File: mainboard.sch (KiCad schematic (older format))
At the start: 69 parts, among them J1 Conn_01x06, J2 USB_B_Micro, J3 xf2m-2415-1a, J4 XF2M-1015-1A, J5 Conn_01x02, J6 U.FL-R-SMT-1, J7 Conn_02x02_Top_Bottom, J8 Micro_SD_Card, SW1 KMR231NG LFS, U1 BMX160, U11 AP2112K-3.3, U2 MAX708RESA-T, U3 ATSAMD51J20A-M, U4 DRV8830DRC, U5 MR25H40, U6 DRV8830DRC, U8 DRV8830DRC, U9 RFM98PW-symbols, Y1 Crystal

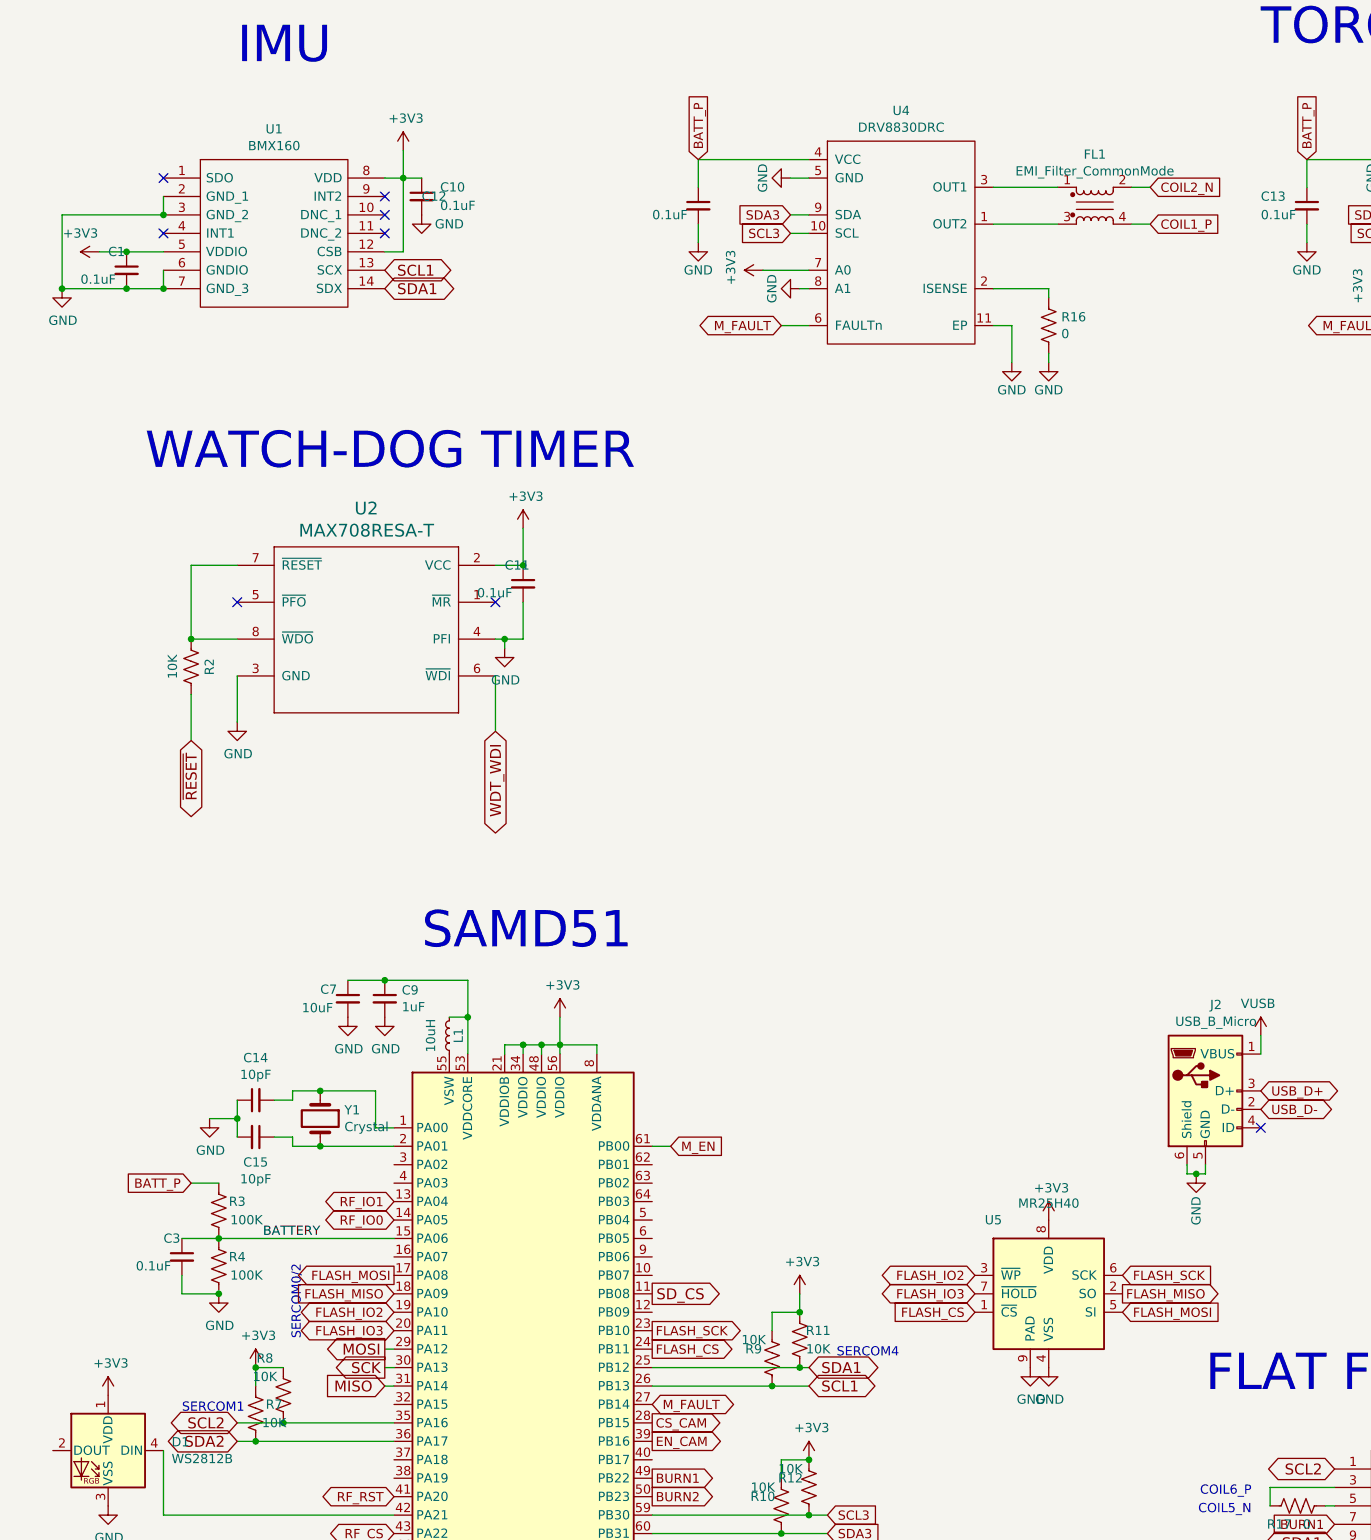
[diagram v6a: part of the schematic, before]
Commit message: ran DRC & added pullups
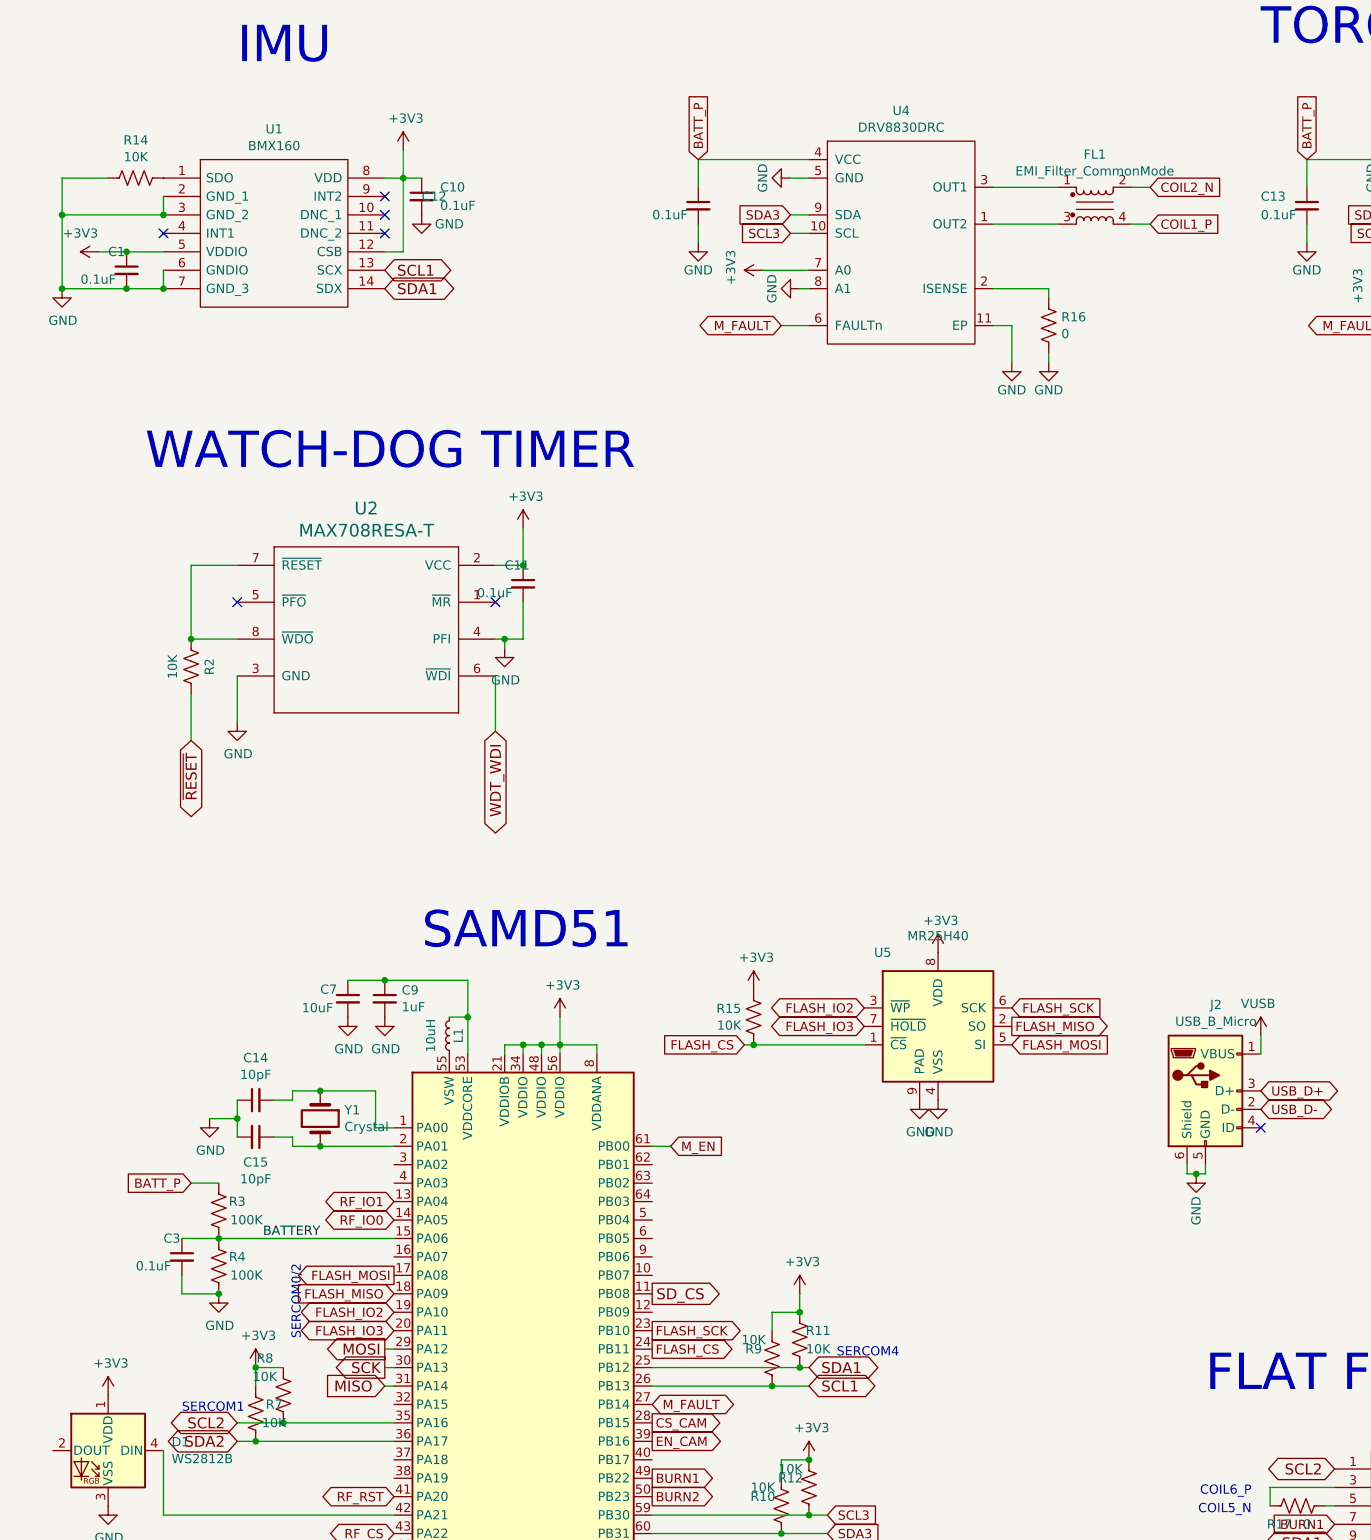
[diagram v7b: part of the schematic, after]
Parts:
- added R14, R15: 10K, Resistor_SMD:R_0402_1005Metric, symbol mainboard-rescue:R_US-Device
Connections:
- net +3V3: now also R15.1
- net FLASH_CS: now also R15.2
- net GND: now also R14.1
- net at U1.1 (SDO): now also R14.2
- no-connect marks 10 -> 9
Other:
- moved on the sheet: U5
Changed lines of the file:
@@
 Wire Wire Line
 	2500 1750 2400 1750
-NoConn ~ 1200 1750
 $Comp
 L mainboard-rescue:R_US-Device R19
@@
 L Memory_NVRAM:MR25H40 U5
 U 1 1 5F5B5E9E
-P 6000 7800
-F 0 "U5" H 5700 8200 50  0000 C CNN
-F 1 "MR25H40" H 6000 8290 50  0000 C CNN
-F 2 "MR25H40:SON127P600X500X90-9N" H 6000 7800 50  0001 C CNN
-F 3 "https://www.everspin.com/file/217/download" H 5700 8100 50  0001 C CNN
-	1    6000 7800
-	1    0    0    -1
-$EndComp
-Text GLabel 5600 7900 0    50   Input ~ 0
+P 5400 6350
+F 0 "U5" H 5100 6750 50  0000 C CNN
+F 1 "MR25H40" H 5400 6840 50  0000 C CNN
+F 2 "MR25H40:SON127P600X500X90-9N" H 5400 6350 50  0001 C CNN
+F 3 "https://www.everspin.com/file/217/download" H 5100 6650 50  0001 C CNN
+	1    5400 6350
+	1    0    0    -1
+$EndComp
+Text GLabel 4350 6450 0    50   Input ~ 0
 FLASH_CS
-Text GLabel 6400 7700 2    50   Input ~ 0
+Text GLabel 5800 6250 2    50   Input ~ 0
 FLASH_SCK
 $Comp
 L power:+3V3 #PWR036
 U 1 1 5F5BBCEF
-P 6000 7400
-F 0 "#PWR036" H 6000 7250 50  0001 C CNN
-F 1 "+3V3" H 6015 7573 50  0000 C CNN
-F 2 "" H 6000 7400 50  0001 C CNN
-F 3 "" H 6000 7400 50  0001 C CNN
-	1    6000 7400
+P 5400 5950
+F 0 "#PWR036" H 5400 5800 50  0001 C CNN
+F 1 "+3V3" H 5415 6123 50  0000 C CNN
+F 2 "" H 5400 5950 50  0001 C CNN
+F 3 "" H 5400 5950 50  0001 C CNN
+	1    5400 5950
 	1    0    0    -1
 $EndComp
@@
 L power:GND #PWR037
 U 1 1 5F5BC9E4
-P 6000 8200
-F 0 "#PWR037" H 6000 7950 50  0001 C CNN
-F 1 "GND" H 6005 8027 50  0000 C CNN
-F 2 "" H 6000 8200 50  0001 C CNN
-F 3 "" H 6000 8200 50  0001 C CNN
-	1    6000 8200
+P 5400 6750
+F 0 "#PWR037" H 5400 6500 50  0001 C CNN
+F 1 "GND" H 5405 6577 50  0000 C CNN
+F 2 "" H 5400 6750 50  0001 C CNN
+F 3 "" H 5400 6750 50  0001 C CNN
+	1    5400 6750
 	1    0    0    -1
 $EndComp
@@
 L power:GND #PWR034
 U 1 1 5F5BD27D
-P 5900 8200
-F 0 "#PWR034" H 5900 7950 50  0001 C CNN
-F 1 "GND" H 5905 8027 50  0000 C CNN
-F 2 "" H 5900 8200 50  0001 C CNN
-F 3 "" H 5900 8200 50  0001 C CNN
-	1    5900 8200
-	1    0    0    -1
-$EndComp
-Text GLabel 5600 7700 0    50   BiDi ~ 0
+P 5300 6750
+F 0 "#PWR034" H 5300 6500 50  0001 C CNN
+F 1 "GND" H 5305 6577 50  0000 C CNN
+F 2 "" H 5300 6750 50  0001 C CNN
+F 3 "" H 5300 6750 50  0001 C CNN
+	1    5300 6750
+	1    0    0    -1
+$EndComp
+Text GLabel 5000 6250 0    50   BiDi ~ 0
 FLASH_IO2
-Text GLabel 5600 7800 0    50   BiDi ~ 0
+Text GLabel 5000 6350 0    50   BiDi ~ 0
 FLASH_IO3
-Text GLabel 6400 7800 2    50   Output ~ 0
+Text GLabel 5800 6350 2    50   Output ~ 0
 FLASH_MISO
-Text GLabel 6400 7900 2    50   Input ~ 0
+Text GLabel 5800 6450 2    50   Input ~ 0
 FLASH_MOSI
 Text Notes 7150 1050 0    197  ~ 0
@@
 Wire Wire Line
 	1600 6850 1600 6950
+$Comp
+L mainboard-rescue:R_US-Device R14
+U 1 1 5F47CA9A
+P 1050 1750
+F 0 "R14" V 1255 1750 50  0000 C CNN
+F 1 "10K" V 1164 1750 50  0000 C CNN
+F 2 "Resistor_SMD:R_0402_1005Metric" V 1090 1740 50  0001 C CNN
+F 3 "~" H 1050 1750 50  0001 C CNN
+	1    1050 1750
+	0    -1   -1   0
+$EndComp
+Wire Wire Line
+	900  1750 650  1750
+Wire Wire Line
+	650  1750 650  1950
+Connection ~ 650  1950
+$Comp
+L mainboard-rescue:R_US-Device R15
+U 1 1 5F48B40E
+P 4400 6300
+F 0 "R15" H 4333 6346 50  0000 R CNN
+F 1 "10K" H 4333 6255 50  0000 R CNN
+F 2 "Resistor_SMD:R_0402_1005Metric" V 4440 6290 50  0001 C CNN
+F 3 "~" H 4400 6300 50  0001 C CNN
+	1    4400 6300
+	1    0    0    -1
+$EndComp
+Wire Wire Line
+	4350 6450 4400 6450
+Connection ~ 4400 6450
+Wire Wire Line
+	4400 6450 5000 6450
+$Comp
+L power:+3V3 #PWR031
+U 1 1 5F4AC667
+P 4400 6150
+F 0 "#PWR031" H 4400 6000 50  0001 C CNN
+F 1 "+3V3" H 4415 6323 50  0000 C CNN
+F 2 "" H 4400 6150 50  0001 C CNN
+F 3 "" H 4400 6150 50  0001 C CNN
+	1    4400 6150
+	1    0    0    -1
+$EndComp
 $EndSCHEMATC

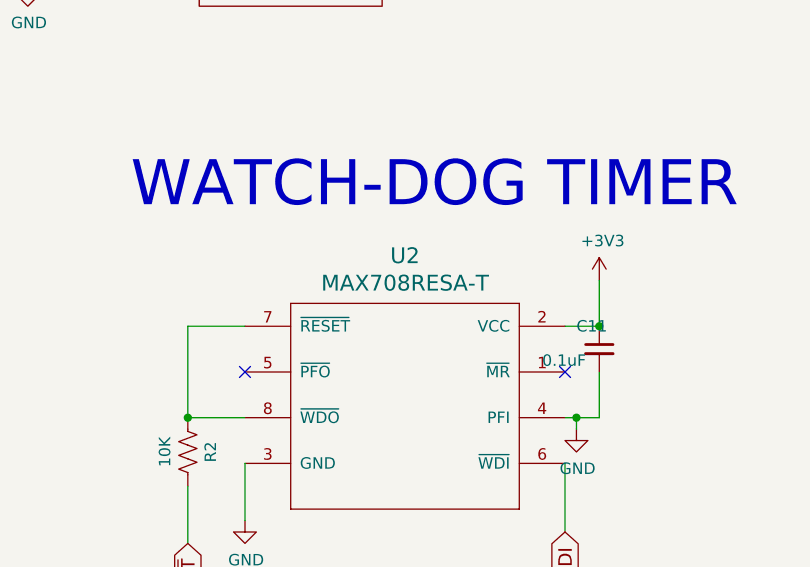
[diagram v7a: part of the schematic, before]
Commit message: fixed WDT part number
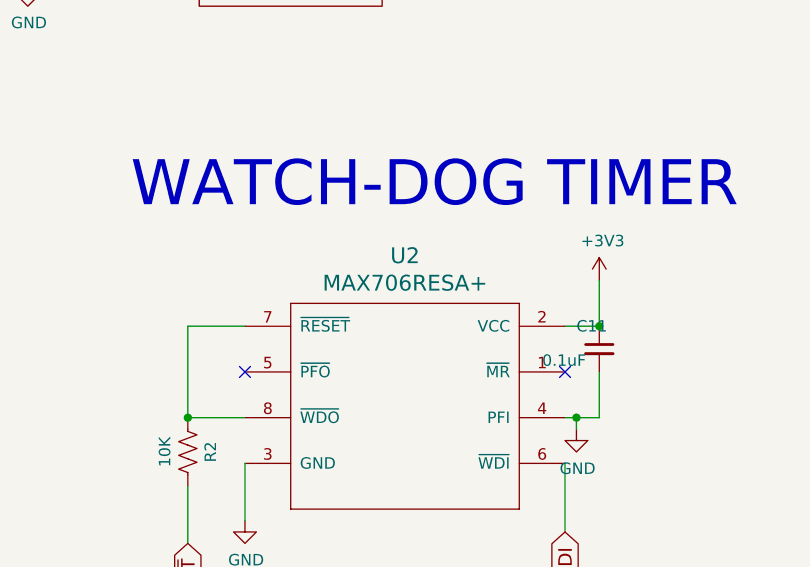
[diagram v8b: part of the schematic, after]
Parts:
- U2: value MAX708RESA-T -> MAX706RESA+
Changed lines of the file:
@@
 P 3100 3950
 F 0 "U2" H 3900 4358 69  0000 C CNN
-F 1 "MAX708RESA-T" H 3900 4238 69  0000 C CNN
+F 1 "MAX706RESA+" H 3900 4238 69  0000 C CNN
 F 2 "Package_SO:SO-8_3.9x4.9mm_P1.27mm" H 3100 3950 50  0001 C CNN
 F 3 "" H 3100 3950 50  0001 C CNN
